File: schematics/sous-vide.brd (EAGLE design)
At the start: 81.3 x 81.3 mm, 31 parts, among them IC1 MEGA8-P, T1 BC547, T2 BC547, T3 BC547

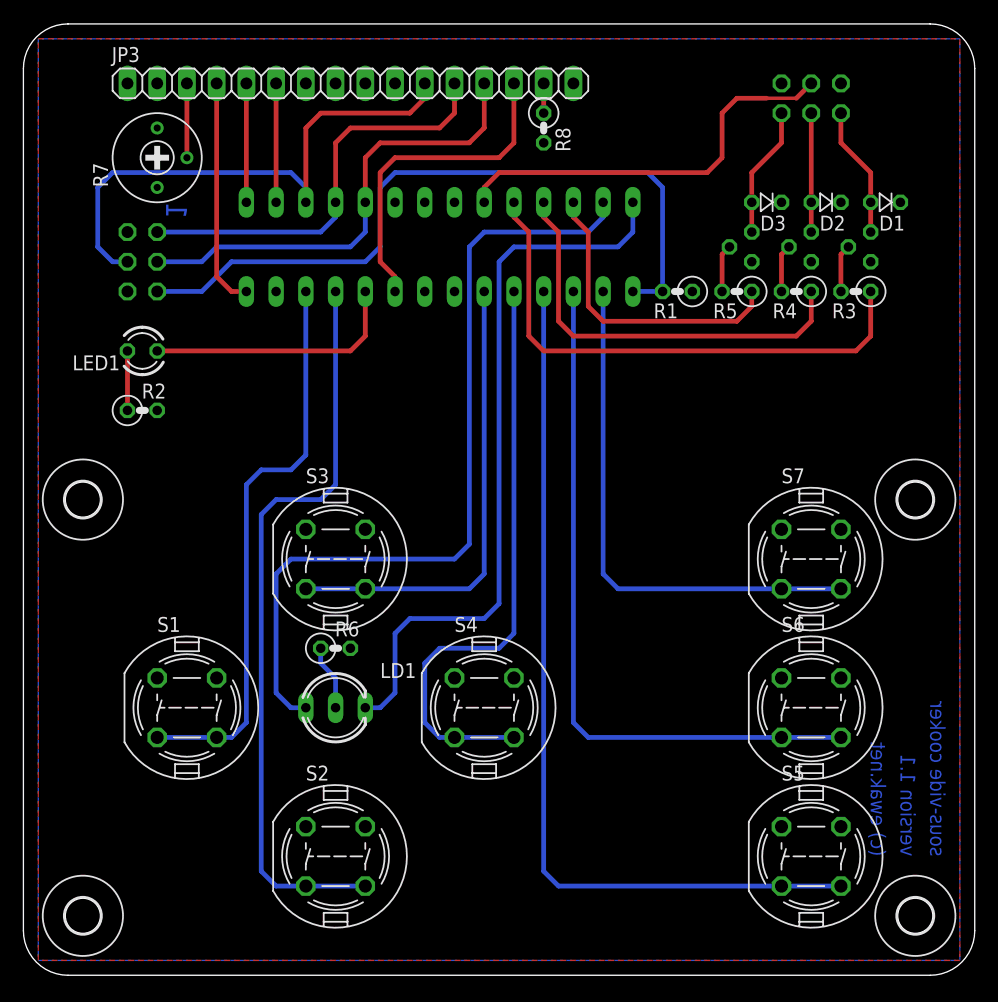
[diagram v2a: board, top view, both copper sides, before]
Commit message: Reworked schema and pcb for new buttons and display.
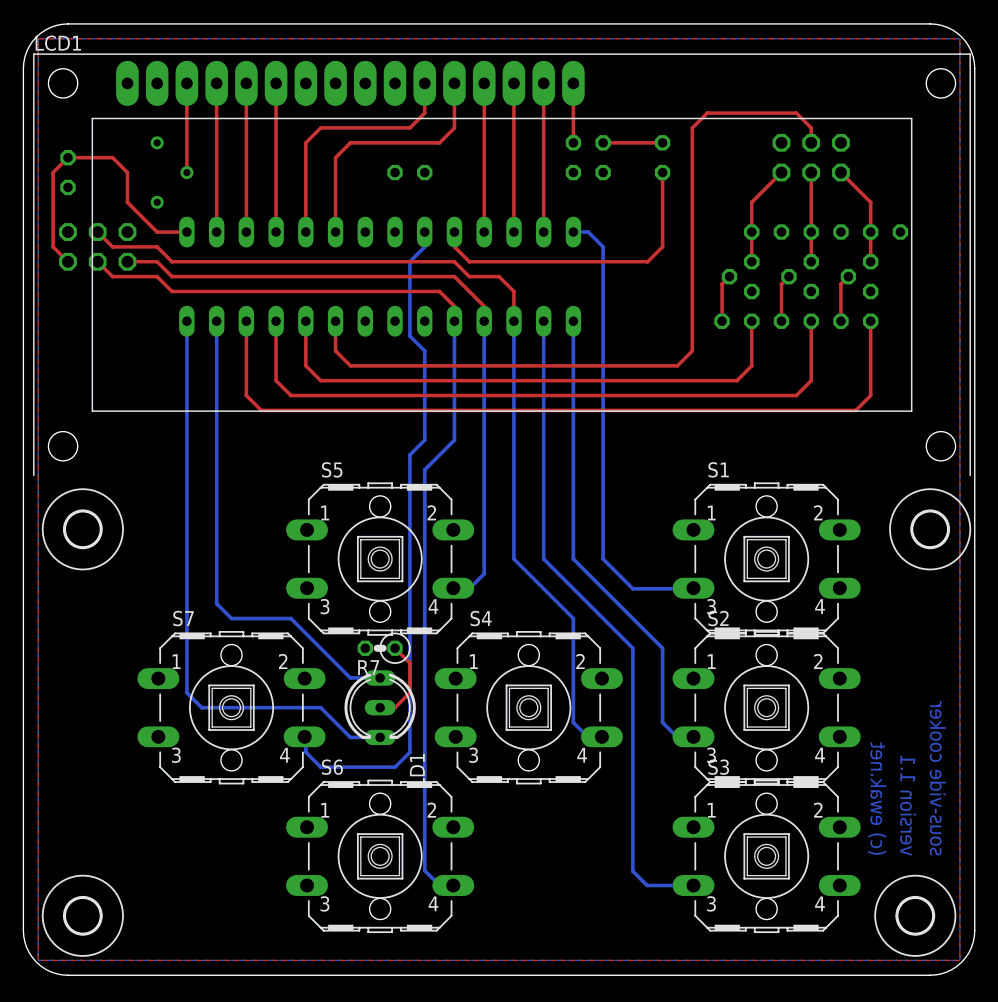
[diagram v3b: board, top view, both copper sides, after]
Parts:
- removed JP1: ISP, pinhead:2X03
- removed JP2: IO, pinhead:2X03
- added C1: 100n, resistor:C025-025X050
- added JP4: ISP, pinhead:2X03
- added LCD1: LCD_2X16_SIL, lcd_2x16_led_backlight:HY-1602F
- JP3: value display -> IO; device pinhead:1X16 -> pinhead:2X03
- R5: value 330 -> (none); device rcl:0207/2V -> resistor:RTRIM3339P
- R7: value (none) -> 330; device resistor:RTRIM3339P -> rcl:0207/2V
- S1, S2, S3, S4, S5, S6, S7: value DT6 -> (none); device switch-misc:DT6 -> switch-omron:B3F-40XX
- moved H2 72.4 mm to (77.5, 38.1)
- moved H3 71.2 mm to (5.08, 38.1)
- moved R1 53.1 mm to (3.81, 68.6), flipped to the bottom, turned to 90 degrees
- moved R2 51.4 mm to (61.0, 55.9), flipped to the bottom
- moved S1 51.1 mm to (63.5, 35.6)
- moved S7 51.1 mm to (17.8, 22.9)
- moved R5 50.6 mm to (11.4, 68.6), flipped to the bottom, turned to 270 degrees
- moved LED1 47.4 mm to (54.6, 69.8), flipped to the bottom, turned to 90 degrees
- moved R6 46.6 mm to (47.0, 69.8), flipped to the bottom, turned to 90 degrees
- moved R7 46.0 mm to (30.5, 27.9), turned to 180 degrees
- moved S3 44.7 mm to (63.5, 10.2)
- moved S5 44.7 mm to (30.5, 35.6)
- moved JP3 39.9 mm to (67.3, 69.8), flipped to the bottom
- moved S2 39.0 mm to (63.5, 22.9)
- moved S6 39.0 mm to (30.5, 10.2)
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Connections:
- removed net N$15 (its old number): JP3.15, R8.1
- removed net N$20: IC1.14, JP3.4
- new net N$2: LCD1.16, R6.2
- new net N$33: IC1.12, LCD1.14
- new net N$34: IC1.13, LCD1.15
- net GND: now also C1.2, JP3.6, JP4.6, LCD1.2, R5.1, R6.1, R7.2, R8.1; no longer JP1.6, JP2.5, JP3.1, JP3.16, R2.2, R6.2, R7.3
- net N$1: now also R8.2; no longer R2.1
- net N$10: now also R2.2; no longer R3.2
- net N$11: now also R3.2; no longer R4.2
- net N$12: now also R4.2; no longer R5.2
- net N$13: now also JP3.5; no longer JP2.6
- net N$14: now also LCD1.3, R5.2; no longer JP3.3, R7.2
- net N$16: now also JP3.3; no longer JP2.4
- net N$17: now also JP3.1; no longer JP2.2
- net N$18: now also JP4.3, S6.4; no longer JP1.3, JP3.13
- net N$19: now also JP4.1, S5.4; no longer JP1.1, JP3.12
- net N$21: now also IC1.2, LCD1.4; no longer IC1.15, JP3.5
- net N$22: now also IC1.3, LCD1.5; no longer IC1.16, JP3.6
- net N$23: now also IC1.4, LCD1.6; no longer IC1.9, JP3.14
- net N$24: now also JP4.4, S4.4; no longer JP1.4, JP3.11
- net N$26: now also IC1.9, S7.4; no longer IC1.12, S1.3, S1.4
- net N$28: now also IC1.5, LCD1.11; no longer IC1.11, S2.3, S2.4
- net N$3: now also JP3.4; no longer JP2.3
- net N$30: now also IC1.6, LCD1.12; no longer IC1.5, S4.3, S4.4
- net N$31: now also JP4.5; no longer JP1.5
- net N$32: now also IC1.11, LCD1.13; no longer IC1.6, S3.3, S3.4
- net N$35: now also IC1.16, S3.3; no longer IC1.4, S5.3, S5.4
- net N$36: now also IC1.14, S1.3; no longer IC1.2, S7.3, S7.4
- net N$37: now also IC1.15, S2.3; no longer IC1.3, S6.3, S6.4
- net N$4: now also R2.1; no longer R3.1
- net N$5: now also R3.1; no longer R4.1
- net N$6: now also R4.1; no longer R5.1
- net N$7: now also R7.1; no longer R6.1
- net VCC: now also C1.1, JP4.2, LCD1.1, R5.3; no longer JP1.2, JP2.1, R7.1, R8.2
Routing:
- net N$18: track 40.2 -> 83.1 mm
- net N$28: track 63.8 -> 21.4 mm
- net N$6: track 25.7 -> 67.1 mm
- net N$31: track 62.3 -> 24.2 mm
- net N$24: track 47.1 -> 79.6 mm
- net N$3: track 35.1 -> 65.6 mm
- net N$30: track 51.1 -> 21.4 mm
- net N$9: track 69.9 -> 40.7 mm
- net N$32: track 39.9 -> 12.7 mm
- net N$19: track 35.9 -> 58.0 mm
- net N$5: track 35.9 -> 56.9 mm
- net N$37: track 60.2 -> 40.6 mm
- net N$35: track 75.5 -> 55.8 mm
- net N$20: track 19.6 -> 0.00 mm
- net N$23: track 28.2 -> 12.7 mm
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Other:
- board text removed: "1"

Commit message: Minor tweaks before shipping to pcb manufacturer.
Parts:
- moved D1 2.54 mm to (61.0, 63.5), turned to 180 degrees
- moved JP4 2.54 mm to (6.35, 59.7)
- moved D2 2.54 mm to (66.0, 63.5), turned to 180 degrees
- moved D3 2.54 mm to (71.1, 63.5), turned to 180 degrees
- flipped R7 to the bottom, turned to 0 degrees
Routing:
- net N$31: track 24.2 -> 26.8 mm
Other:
- board text added: "1"
- board text added: "version 1.2"
- board text removed: "version 1.1"

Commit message: Fixed VCC/VDD/VSS/GND issue with display, renumbered parts, updated port assignment in code.
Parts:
- R1: value 100k -> 10k
- R2, R3, R4, R6, R7, R8: value 330 -> 180
- R5: value (none) -> 10k
- renumbered JP3 to JP1, JP4 to JP2
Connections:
- net GND: now also LCD1.1, R5.3; no longer LCD1.2, R5.1
- net VCC: now also LCD1.2, R5.1; no longer LCD1.1, R5.3
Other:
- board text added: "version 1.3"
- board text removed: "version 1.2"
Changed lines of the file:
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@@
 <text x="21.59" y="7.62" size="1.27" layer="25" font="vector" rot="R180">(c) ewak.net</text>
 <text x="21.59" y="12.7" size="1.27" layer="25" font="vector" rot="R180">sous-vide cooker</text>
-<text x="21.59" y="10.16" size="1.27" layer="25" font="vector" rot="R180">version 1.2</text>
+<text x="21.59" y="10.16" size="1.27" layer="25" font="vector" ratio="5" rot="R180">version 1.3</text>
 </plain>
 <attributes>
@@
 </autorouter>
 <elements>
-<element name="R1" library="rcl" package="0207/2V" value="100k" x="3.81" y="68.58" smashed="yes" rot="MR90">
+<element name="R1" library="rcl" package="0207/2V" value="10k" x="3.81" y="68.58" smashed="yes" rot="MR90">
 <attribute name="NAME" x="5.08" y="64.77" size="1.27" layer="26" ratio="10" rot="MR0"/>
 </element>
-<element name="R7" library="rcl" package="0207/2V" value="330" x="30.48" y="27.94" smashed="yes" rot="MR0">
+<element name="R7" library="rcl" package="0207/2V" value="180" x="30.48" y="27.94" smashed="yes" rot="MR0">
 <attribute name="NAME" x="27.94" y="27.94" size="1.27" layer="26" ratio="10" rot="MR0"/>
 </element>
-<element name="R5" library="resistor" package="RTRIM3339P" value="" x="11.43" y="68.58" smashed="yes" rot="MR270">
+<element name="R5" library="resistor" package="RTRIM3339P" value="10k" x="11.43" y="68.58" smashed="yes" rot="MR270">
 <attribute name="NAME" x="8.89" y="64.77" size="1.27" layer="26" rot="MR0"/>
 <attribute name="VALUE" x="17.035" y="71.095" size="1.27" layer="28" rot="MR270"/>
 </element>
-<element name="R6" library="rcl" package="0207/2V" value="330" x="46.99" y="69.85" smashed="yes" rot="MR90">
+<element name="R6" library="rcl" package="0207/2V" value="180" x="46.99" y="69.85" smashed="yes" rot="MR90">
 <attribute name="NAME" x="48.26" y="66.04" size="1.27" layer="26" ratio="10" rot="MR0"/>
 </element>
@@
 <element name="H2" library="holes" package="3,0" value="MOUNT-HOLE3.0" x="77.47" y="38.1"/>
 <element name="H4" library="holes" package="3,0" value="MOUNT-HOLE3.0" x="5.08" y="5.08" smashed="yes"/>
-<element name="JP4" library="pinhead" package="2X03" value="ISP" x="6.35" y="59.69" smashed="yes" rot="MR0">
+<element name="JP2" library="pinhead" package="2X03" value="ISP" x="6.35" y="59.69" smashed="yes" rot="MR0">
 <attribute name="NAME" x="2.54" y="57.15" size="1.27" layer="26" ratio="10" rot="MR180"/>
 </element>
@@
 <attribute name="VALUE" x="52.959" y="71.755" size="1.27" layer="28" ratio="10" rot="MR90"/>
 </element>
-<element name="R8" library="rcl" package="0207/2V" value="330" x="49.53" y="69.85" smashed="yes" rot="MR90">
+<element name="R8" library="rcl" package="0207/2V" value="180" x="49.53" y="69.85" smashed="yes" rot="MR90">
 <attribute name="NAME" x="50.8" y="66.04" size="1.27" layer="26" ratio="10" rot="MR0"/>
 </element>
@@
 <attribute name="VALUE" x="69.469" y="65.913" size="1.27" layer="28" ratio="10" rot="MR180"/>
 </element>
-<element name="R2" library="rcl" package="0207/2V" value="330" x="60.96" y="55.88" smashed="yes" rot="MR0">
+<element name="R2" library="rcl" package="0207/2V" value="180" x="60.96" y="55.88" smashed="yes" rot="MR0">
 <attribute name="NAME" x="63.5" y="53.34" size="1.27" layer="26" ratio="10" rot="MR0"/>
 </element>
-<element name="R3" library="rcl" package="0207/2V" value="330" x="66.04" y="55.88" smashed="yes" rot="MR0">
+<element name="R3" library="rcl" package="0207/2V" value="180" x="66.04" y="55.88" smashed="yes" rot="MR0">
 <attribute name="NAME" x="68.58" y="53.34" size="1.27" layer="26" ratio="10" rot="MR0"/>
 </element>
-<element name="R4" library="rcl" package="0207/2V" value="330" x="71.12" y="55.88" smashed="yes" rot="MR0">
+<element name="R4" library="rcl" package="0207/2V" value="180" x="71.12" y="55.88" smashed="yes" rot="MR0">
 <attribute name="NAME" x="73.66" y="53.34" size="1.27" layer="26" ratio="10" rot="MR0"/>
 </element>
-<element name="JP3" library="pinhead" package="2X03" value="IO" x="67.31" y="69.85" smashed="yes" rot="MR0">
+<element name="JP1" library="pinhead" package="2X03" value="IO" x="67.31" y="69.85" smashed="yes" rot="MR0">
 <attribute name="NAME" x="71.12" y="72.39" size="1.27" layer="26" ratio="10" rot="MR180"/>
 </element>
@@
 <signal name="GND">
 <polygon width="0.4064" layer="16" orphans="yes">
-<vertex x="1.27" y="80.01"/>
-<vertex x="1.27" y="1.27"/>
-<vertex x="80.01" y="1.27"/>
-<vertex x="80.01" y="80.01"/>
+<vertex x="1.27" y="76.4179"/>
+<vertex x="1.27" y="4.8621" curve="90"/>
+<vertex x="4.8621" y="1.27"/>
+<vertex x="76.4179" y="1.27" curve="90"/>
+<vertex x="80.01" y="4.8621"/>
+<vertex x="80.01" y="76.4179" curve="90"/>
+<vertex x="76.4179" y="80.01"/>
+<vertex x="4.8621" y="80.01" curve="90"/>
 </polygon>
-<contactref element="JP4" pad="6"/>
+<contactref element="JP2" pad="6"/>
 <contactref element="IC1" pad="8"/>
 <contactref element="IC1" pad="22"/>
@@
 <contactref element="R7" pad="2"/>
 <contactref element="R6" pad="1"/>
-<contactref element="R5" pad="1"/>
-<contactref element="LCD1" pad="2"/>
 <contactref element="S7" pad="1"/>
 <contactref element="S7" pad="2"/>
@@
 <contactref element="C1" pad="2"/>
 <contactref element="R8" pad="1"/>
-<contactref element="JP3" pad="6"/>
+<contactref element="JP1" pad="6"/>
+<contactref element="R5" pad="3"/>
+<contactref element="LCD1" pad="1"/>
 </signal>
 <signal name="VCC">
 <polygon width="0.4064" layer="1" orphans="yes">
-<vertex x="1.27" y="80.01"/>
-<vertex x="80.01" y="80.01"/>
-<vertex x="80.01" y="1.27"/>
-<vertex x="1.27" y="1.27"/>
+<vertex x="76.4179" y="1.27"/>
+<vertex x="4.8621" y="1.27" curve="-90"/>
+<vertex x="1.27" y="4.8621"/>
+<vertex x="1.27" y="76.4179" curve="-90"/>
+<vertex x="4.8621" y="80.01"/>
+<vertex x="76.4179" y="80.01" curve="-90"/>
+<vertex x="80.01" y="76.4179"/>
+<vertex x="80.01" y="4.8621" curve="-90"/>
 </polygon>
-<contactref element="JP4" pad="2"/>
+<contactref element="JP2" pad="2"/>
 <contactref element="IC1" pad="7"/>
 <contactref element="IC1" pad="20"/>
 <contactref element="IC1" pad="21"/>
 <contactref element="R1" pad="1"/>
-<contactref element="LCD1" pad="1"/>
-<contactref element="R5" pad="3"/>
 <contactref element="C1" pad="1"/>
 <contactref element="D2" pad="C"/>
 <contactref element="D3" pad="C"/>
-<contactref element="JP3" pad="2"/>
+<contactref element="JP1" pad="2"/>
 <contactref element="D1" pad="C"/>
+<contactref element="LCD1" pad="2"/>
+<contactref element="R5" pad="1"/>
 </signal>
 <signal name="N$19">
 <contactref element="IC1" pad="18"/>
-<contactref element="JP4" pad="1"/>
+<contactref element="JP2" pad="1"/>
 <wire x1="39.37" y1="55.88" x2="39.37" y2="34.29" width="0.3048" layer="16"/>
 <wire x1="39.37" y1="34.29" x2="38.1" y2="33.02" width="0.3048" layer="16"/>
@@
 </signal>
 <signal name="N$31">
-<contactref element="JP4" pad="5"/>
+<contactref element="JP2" pad="5"/>
 <contactref element="R1" pad="2"/>
 <contactref element="IC1" pad="1"/>
@@
 <signal name="N$3">
 <contactref element="IC1" pad="23"/>
-<contactref element="JP3" pad="4"/>
+<contactref element="JP1" pad="4"/>
 <wire x1="67.31" y1="71.12" x2="67.31" y2="72.39" width="0.3048" layer="1"/>
 <wire x1="67.31" y1="72.39" x2="66.04" y2="73.66" width="0.3048" layer="1"/>
@@
 <signal name="N$24">
 <contactref element="IC1" pad="17"/>
-<contactref element="JP4" pad="4"/>
+<contactref element="JP2" pad="4"/>
 <wire x1="6.35" y1="60.96" x2="7.62" y2="59.69" width="0.3048" layer="1"/>
 <wire x1="7.62" y1="59.69" x2="11.43" y2="59.69" width="0.3048" layer="1"/>
@@
 <wire x1="46.99" y1="76.2" x2="46.99" y2="71.12" width="0.3048" layer="1"/>
 </signal>
-<signal name="N$14">
-<contactref element="R5" pad="2"/>
-<contactref element="LCD1" pad="3"/>
-<wire x1="13.97" y1="76.2" x2="13.97" y2="68.58" width="0.3048" layer="1"/>
-</signal>
 <signal name="N$15">
 <contactref element="LED1" pad="A"/>
@@
 <wire x1="62.23" y1="66.04" x2="62.23" y2="63.5" width="0.3048" layer="1"/>
 <wire x1="62.23" y1="63.5" x2="62.23" y2="60.96" width="0.3048" layer="1"/>
-<contactref element="JP3" pad="5"/>
+<contactref element="JP1" pad="5"/>
 <wire x1="64.77" y1="68.58" x2="62.23" y2="66.04" width="0.3048" layer="1"/>
 </signal>
@@
 <contactref element="D2" pad="A"/>
 <wire x1="67.31" y1="60.96" x2="67.31" y2="63.5" width="0.3048" layer="1"/>
-<contactref element="JP3" pad="3"/>
+<contactref element="JP1" pad="3"/>
 <wire x1="67.31" y1="68.58" x2="67.31" y2="63.5" width="0.3048" layer="1"/>
 </signal>
@@
 <wire x1="72.39" y1="66.04" x2="72.39" y2="63.5" width="0.3048" layer="1"/>
 <wire x1="72.39" y1="63.5" x2="72.39" y2="60.96" width="0.3048" layer="1"/>
-<contactref element="JP3" pad="1"/>
+<contactref element="JP1" pad="1"/>
 <wire x1="69.85" y1="68.58" x2="72.39" y2="66.04" width="0.3048" layer="1"/>
 </signal>
@@
 <signal name="N$18">
 <contactref element="IC1" pad="19"/>
-<contactref element="JP4" pad="3"/>
+<contactref element="JP2" pad="3"/>
 <contactref element="S6" pad="4"/>
 <wire x1="34.29" y1="43.18" x2="34.29" y2="8.9408" width="0.3048" layer="16"/>
@@
 <wire x1="35.56" y1="7.6708" x2="36.7284" y2="7.6708" width="0" layer="19" extent="16-16"/>
 </signal>
+<signal name="N$14">
+<contactref element="R5" pad="2"/>
+<contactref element="LCD1" pad="3"/>
+<wire x1="13.97" y1="68.58" x2="13.97" y2="76.2" width="0.3048" layer="1"/>
+</signal>
 </signals>
